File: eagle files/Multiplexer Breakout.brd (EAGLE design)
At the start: 50.8 x 97.5 mm, 19 parts

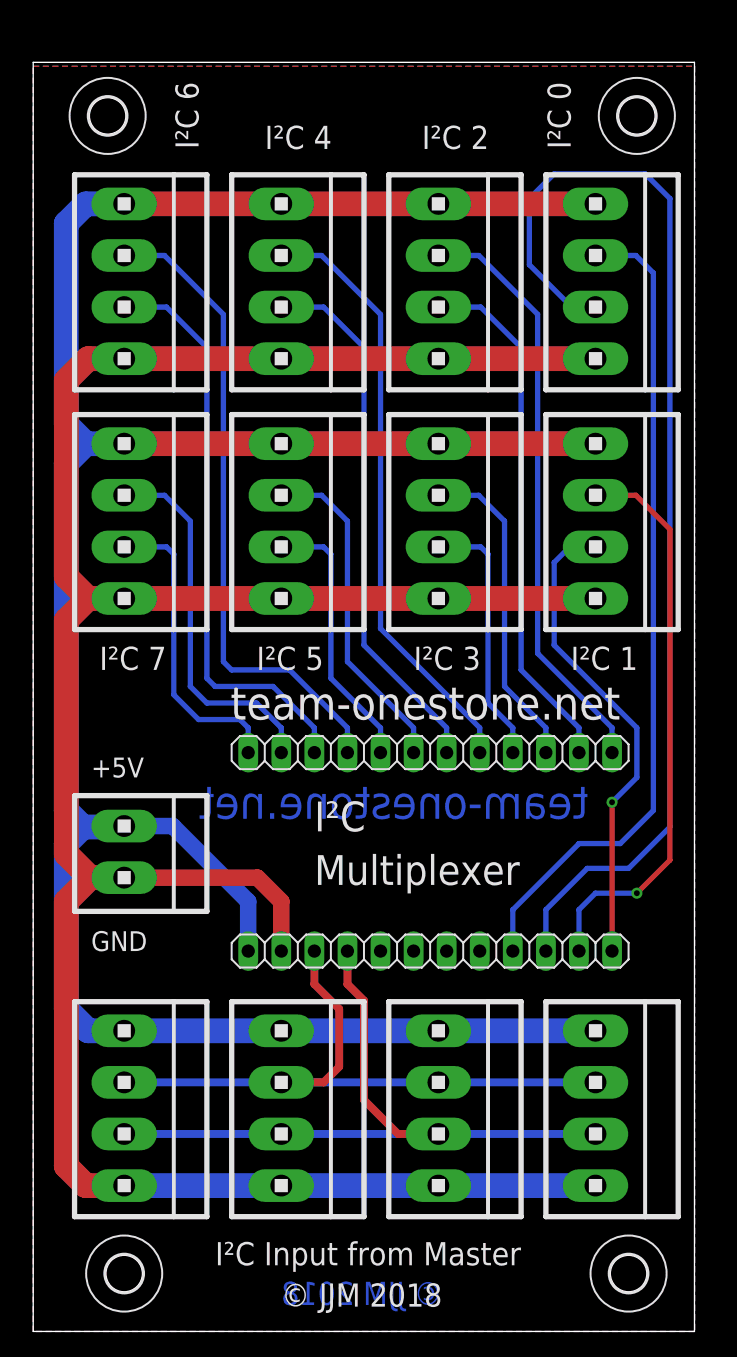
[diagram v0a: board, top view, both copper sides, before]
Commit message: Auf kleinere Stecker umgebaut
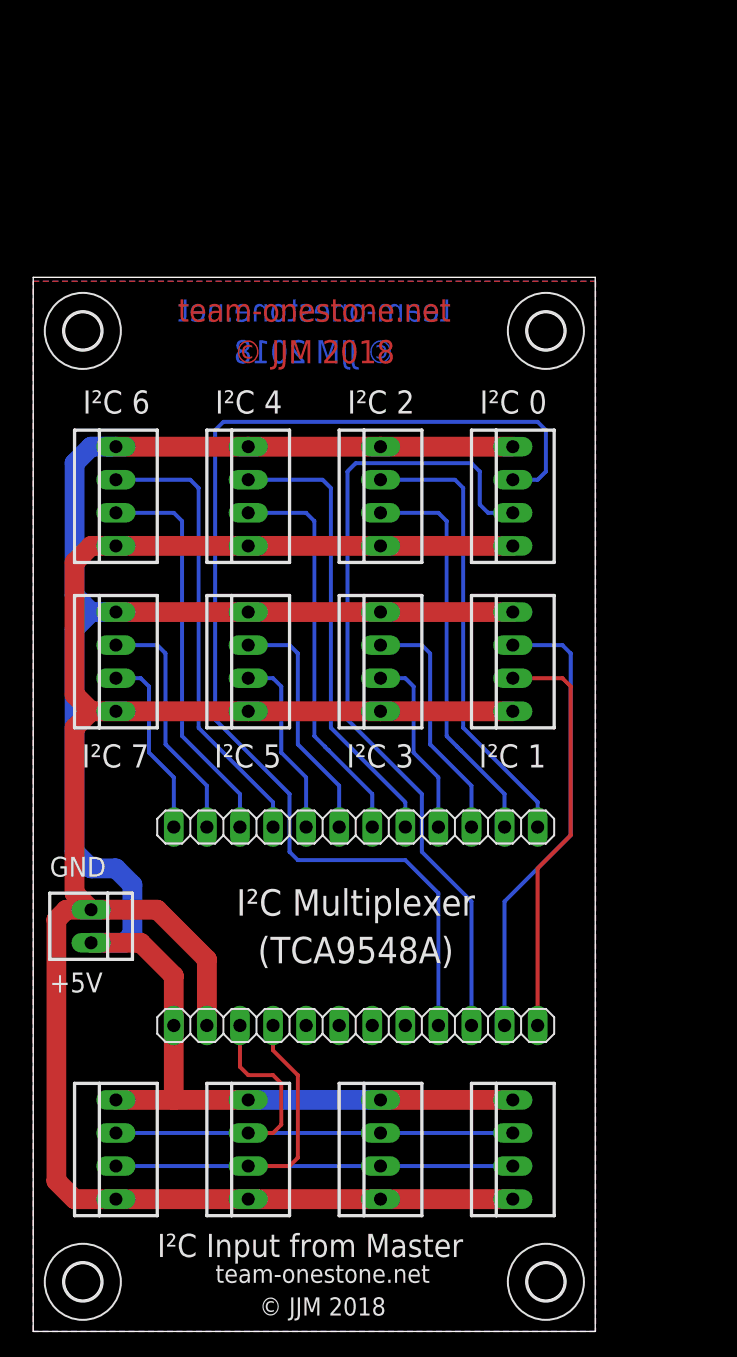
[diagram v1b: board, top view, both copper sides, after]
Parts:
- removed J1, J10, J11, J12, J2, J3, J4, J5, J6, J7, J8, J9: (no value), con-amp:1X4MTA
- removed J13: (no value), con-amp:1X2MTA
- added X1, X10, X11, X12, X2, X3, X4, X5, X6, X7, X8, X9: 22-23-2041, con-molex:22-23-2041
- added X13: 22-23-2021, con-molex:22-23-2021
- moved H3 17.9 mm to (39.4, 76.8)
- moved H4 16.6 mm to (3.81, 76.8)
- moved JP2 8.08 mm to (24.8, 38.7)
- moved JP1 8.08 mm to (24.8, 23.5)
- moved H2 6.38 mm to (39.4, 3.81)
- moved H1 3.24 mm to (3.81, 3.81)
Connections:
- net +5V: now also X1.4, X10.4, X11.4, X12.4, X13.2, X2.4, X3.4, X4.4, X5.4, X6.4, X7.4, X8.4, X9.4; no longer J1.4, J10.4, J11.4, J12.4, J13.2, J2.4, J3.4, J4.4, J5.4, J6.4, J7.4, J8.4, J9.4
- net GND: now also X1.1, X10.1, X11.1, X12.1, X13.1, X2.1, X3.1, X4.1, X5.1, X6.1, X7.1, X8.1, X9.1; no longer J1.1, J10.1, J11.1, J12.1, J13.1, J2.1, J3.1, J4.1, J5.1, J6.1, J7.1, J8.1, J9.1
- net SCL: now also X10.2, X11.2, X12.2, X9.2; no longer J1.2, J2.2, J3.2, J4.2
- net SCL0: now also X1.2; no longer J5.2
- net SCL1: now also X2.2; no longer J6.2
- net SCL2: now also X3.2; no longer J7.2
- net SCL3: now also X4.2; no longer J8.2
- net SCL4: now also X5.2; no longer J9.2
- net SCL5: now also X6.2; no longer J10.2
- net SCL6: now also X7.2; no longer J11.2
- net SCL7: now also X8.2; no longer J12.2
- net SDA: now also X10.3, X11.3, X12.3, X9.3; no longer J1.3, J2.3, J3.3, J4.3
- net SDA0: now also X1.3; no longer J5.3
- net SDA1: now also X2.3; no longer J6.3
- net SDA2: now also X3.3; no longer J7.3
- net SDA3: now also X4.3; no longer J8.3
- net SDA4: now also X5.3; no longer J9.3
- net SDA5: now also X6.3; no longer J10.3
- net SDA6: now also X7.3; no longer J11.3
- net SDA7: now also X8.3; no longer J12.3
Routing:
- net +5V: track 203.3 -> 157.6 mm
- net GND: track 204.0 -> 169.7 mm
- net SDA0: track 63.4 -> 89.6 mm
- net SCL0: track 87.5 -> 62.5 mm
- net SDA6: track 49.7 -> 35.0 mm
- net SCL6: track 44.8 -> 30.7 mm
- net SDA4: track 46.3 -> 35.0 mm
- net SCL4: track 41.4 -> 30.7 mm
- net SDA2: track 45.5 -> 35.0 mm
- net SDA7: track 28.8 -> 18.7 mm
- net SCL2: track 40.6 -> 30.7 mm
- net SCL: track 54.9 -> 45.5 mm
- net SCL7: track 23.5 -> 14.4 mm
- net SDA1: track 43.9 -> 35.4 mm, vias 1 -> 0
- net SDA: track 50.8 -> 43.3 mm
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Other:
- board size 50.8 x 97.5 mm -> 43.2 x 81 mm
- board text added: "I²C Multiplexer (TCA9548A)"
- board text added: "team-onestone.net © JJM 2018"
- board text removed: "I²C Multiplexer"
- board text removed: "team-onestone.net"
- board text removed: "© JJM 2018"
